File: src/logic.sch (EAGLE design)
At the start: 66 parts, among them CON1 CON-4P-TABS-JST_GH-RA, CON11 PINHEAD_1X04-2, CON12 PINHEAD_1X04-2, CON2 PINHEAD_1X04-2.54, CON3 PINHEAD_2X04-PLS-2, CON6 PINHEAD_2X02-PTH-2-MALE, CON7 PINHEAD_2X02-PTH-2-MALE, IC1 STM32F105RCT6, IC10 LM75-TSSOP8, IC11 LM75-TSSOP8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

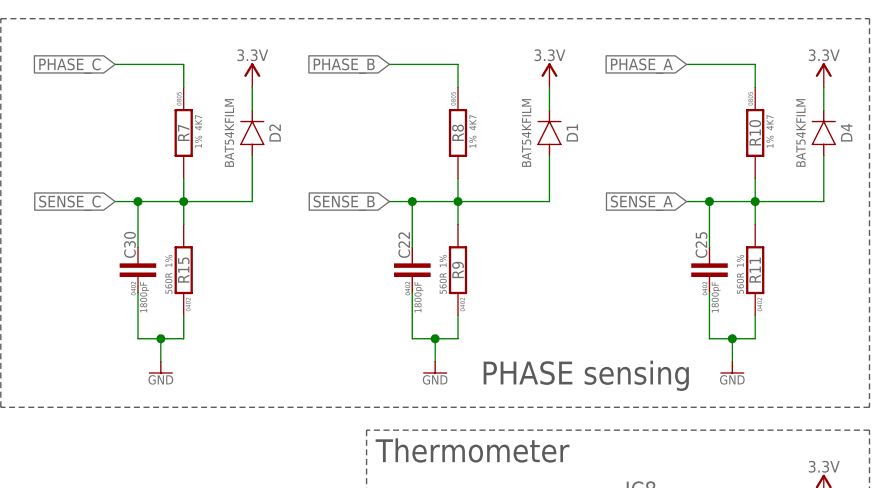
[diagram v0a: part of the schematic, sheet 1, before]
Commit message: BEMF sensig nets updates
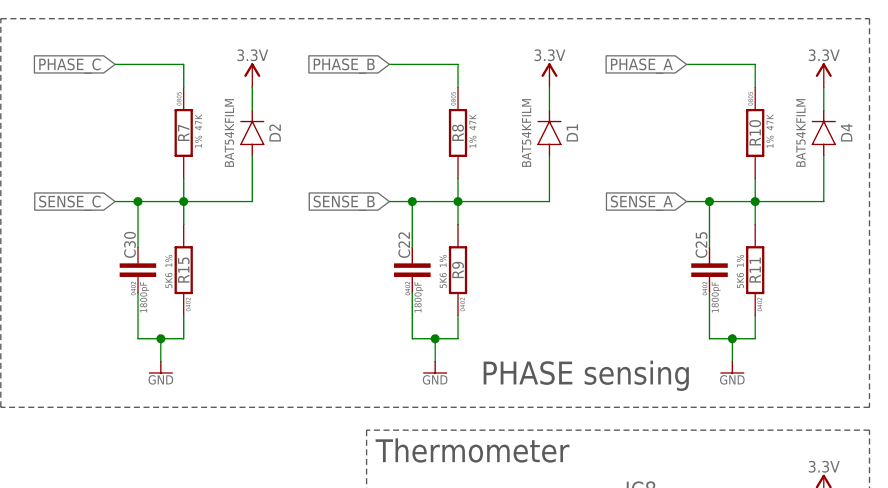
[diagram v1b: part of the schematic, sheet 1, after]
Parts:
- R10, R7, R8: value 4K7 -> 47K
- R11, R15, R9: value 560R -> 5K6
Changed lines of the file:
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@@
 </part>
 <part name="C30" library="rc" library_urn="urn:adsk.eagle:library:2539423" deviceset="C" device="-0402" package3d_urn="urn:adsk.eagle:package:2539461/2" value="1800pF"/>
-<part name="R7" library="rc" library_urn="urn:adsk.eagle:library:2539423" deviceset="R" device="-0805" package3d_urn="urn:adsk.eagle:package:2539455/2" technology="-1%" value="4K7"/>
-<part name="R15" library="rc" library_urn="urn:adsk.eagle:library:2539423" deviceset="R" device="-0402" package3d_urn="urn:adsk.eagle:package:2539456/2" technology="-1%" value="560R"/>
+<part name="R7" library="rc" library_urn="urn:adsk.eagle:library:2539423" deviceset="R" device="-0805" package3d_urn="urn:adsk.eagle:package:2539455/2" technology="-1%" value="47K"/>
+<part name="R15" library="rc" library_urn="urn:adsk.eagle:library:2539423" deviceset="R" device="-0402" package3d_urn="urn:adsk.eagle:package:2539456/2" technology="-1%" value="5K6"/>
 <part name="GND37" library="supply_symbols" library_urn="urn:adsk.eagle:library:13097679" deviceset="GND" device="" value="GND"/>
 <part name="C22" library="rc" library_urn="urn:adsk.eagle:library:2539423" deviceset="C" device="-0402" package3d_urn="urn:adsk.eagle:package:2539461/2" value="1800pF"/>
-<part name="R8" library="rc" library_urn="urn:adsk.eagle:library:2539423" deviceset="R" device="-0805" package3d_urn="urn:adsk.eagle:package:2539455/2" technology="-1%" value="4K7"/>
-<part name="R9" library="rc" library_urn="urn:adsk.eagle:library:2539423" deviceset="R" device="-0402" package3d_urn="urn:adsk.eagle:package:2539456/2" technology="-1%" value="560R"/>
+<part name="R8" library="rc" library_urn="urn:adsk.eagle:library:2539423" deviceset="R" device="-0805" package3d_urn="urn:adsk.eagle:package:2539455/2" technology="-1%" value="47K"/>
+<part name="R9" library="rc" library_urn="urn:adsk.eagle:library:2539423" deviceset="R" device="-0402" package3d_urn="urn:adsk.eagle:package:2539456/2" technology="-1%" value="5K6"/>
 <part name="GND26" library="supply_symbols" library_urn="urn:adsk.eagle:library:13097679" deviceset="GND" device="" value="GND"/>
 <part name="C25" library="rc" library_urn="urn:adsk.eagle:library:2539423" deviceset="C" device="-0402" package3d_urn="urn:adsk.eagle:package:2539461/2" value="1800pF"/>
-<part name="R10" library="rc" library_urn="urn:adsk.eagle:library:2539423" deviceset="R" device="-0805" package3d_urn="urn:adsk.eagle:package:2539455/2" technology="-1%" value="4K7"/>
-<part name="R11" library="rc" library_urn="urn:adsk.eagle:library:2539423" deviceset="R" device="-0402" package3d_urn="urn:adsk.eagle:package:2539456/2" technology="-1%" value="560R"/>
+<part name="R10" library="rc" library_urn="urn:adsk.eagle:library:2539423" deviceset="R" device="-0805" package3d_urn="urn:adsk.eagle:package:2539455/2" technology="-1%" value="47K"/>
+<part name="R11" library="rc" library_urn="urn:adsk.eagle:library:2539423" deviceset="R" device="-0402" package3d_urn="urn:adsk.eagle:package:2539456/2" technology="-1%" value="5K6"/>
 <part name="GND27" library="supply_symbols" library_urn="urn:adsk.eagle:library:13097679" deviceset="GND" device="" value="GND"/>
 <part name="+P7" library="supply_symbols" library_urn="urn:adsk.eagle:library:5017758" deviceset="3.3V" device=""/>

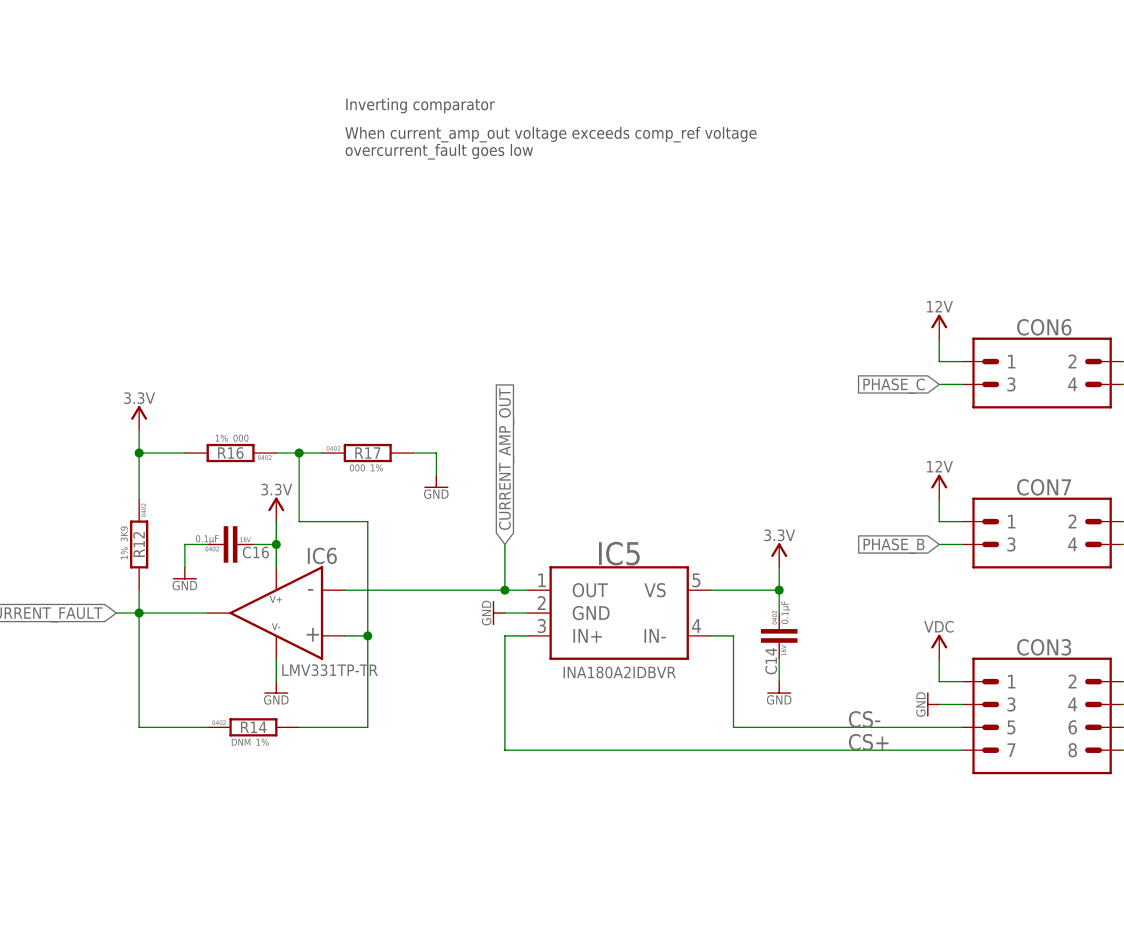
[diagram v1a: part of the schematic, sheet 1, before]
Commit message: Current amplifier input filtering added
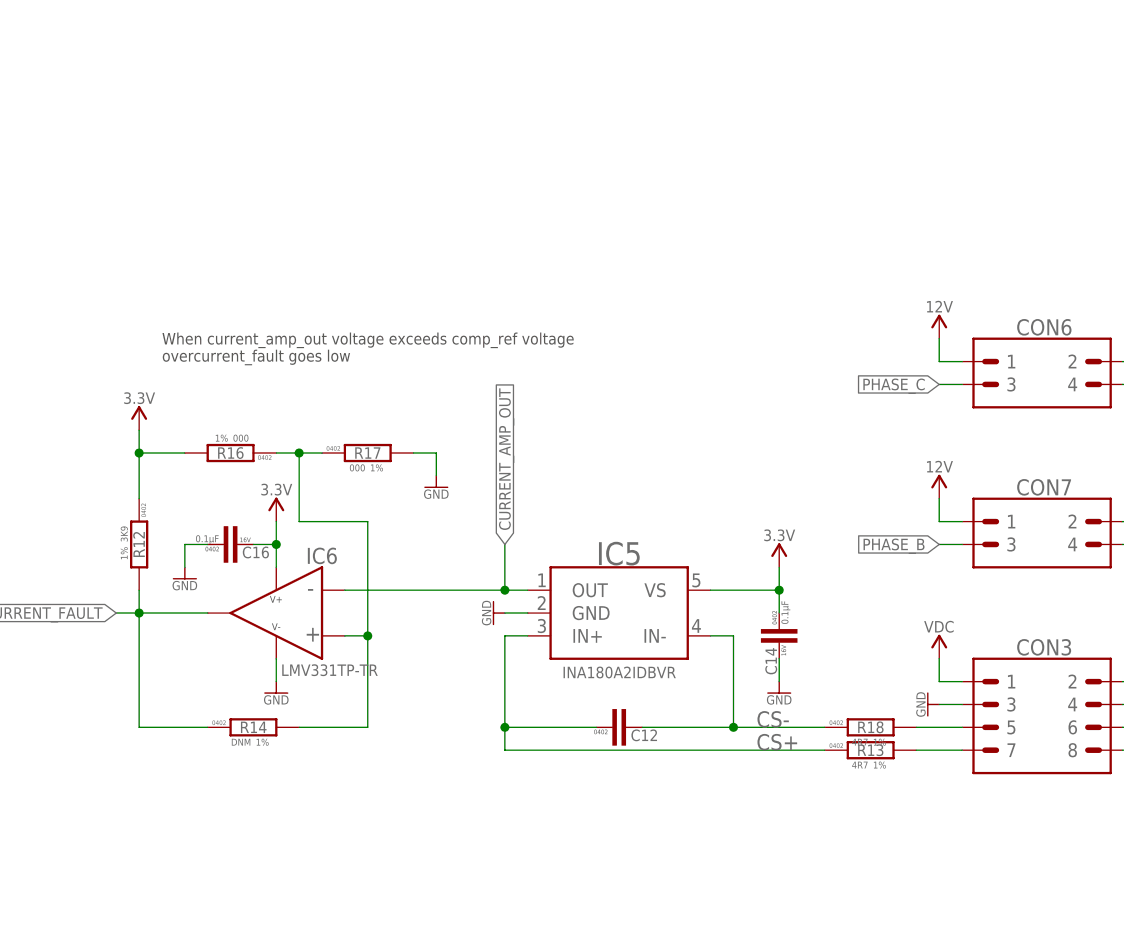
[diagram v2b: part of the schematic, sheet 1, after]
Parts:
- added C12: (no value), rc:C-0402
- added R13, R18: 4R7, rc:R-1%-0402
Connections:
- new net N$4: CON3.5, R18.2
- net CS+: now also C12.1, R13.1; no longer CON3.7
- net CS-: now also C12.2, R18.1; no longer CON3.5
- net N$1: now also CON3.7, R13.2
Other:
- note removed: "Inverting comparator"
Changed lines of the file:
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@@
 <part name="GND48" library="supply_symbols" library_urn="urn:adsk.eagle:library:13097679" deviceset="GND" device="" value="GND"/>
 <part name="+P15" library="supply_symbols" library_urn="urn:adsk.eagle:library:5017758" deviceset="5V" device=""/>
+<part name="R13" library="rc" library_urn="urn:adsk.eagle:library:2539423" deviceset="R" device="-0402" package3d_urn="urn:adsk.eagle:package:2539456/2" technology="-1%" value="4R7"/>
+<part name="R18" library="rc" library_urn="urn:adsk.eagle:library:2539423" deviceset="R" device="-0402" package3d_urn="urn:adsk.eagle:package:2539456/2" technology="-1%" value="4R7"/>
+<part name="C12" library="rc" library_urn="urn:adsk.eagle:library:2539423" deviceset="C" device="-0402" package3d_urn="urn:adsk.eagle:package:2539461/2"/>
 </parts>
 <sheets>
@@
 <text x="142.24" y="55.88" size="1.27" layer="97" font="vector">Place R26 TO WRITE PROTECT</text>
 <text x="142.24" y="33.02" size="1.778" layer="97">WP pin pull up is optional</text>
-<text x="129.54" y="243.84" size="1.27" layer="97" font="vector">Inverting comparator</text>
-<text x="129.54" y="238.76" size="1.27" layer="97" font="vector">When current_amp_out voltage exceeds comp_ref voltage
+<text x="109.22" y="215.9" size="1.27" layer="97" font="vector">When current_amp_out voltage exceeds comp_ref voltage
 overcurrent_fault goes low</text>
 </plain>
@@
 <instance part="GND44" gate="1" x="139.7" y="203.2" smashed="yes">
 <attribute name="VALUE" x="139.7" y="201.168" size="1.016" layer="96" font="vector" ratio="15" align="center"/>
+</instance>
+<instance part="R13" gate="G$1" x="187.96" y="172.72" smashed="yes">
+<attribute name="NAME" x="187.96" y="172.72" size="1.27" layer="95" font="vector" align="center"/>
+<attribute name="VALUE" x="187.706" y="170.688" size="0.762" layer="96" font="vector" align="bottom-right"/>
+<attribute name="PACKAGE" x="184.15" y="173.228" size="0.508" layer="95" font="vector" align="center"/>
+<attribute name="TOLERANCE" x="188.214" y="170.688" size="0.762" layer="96" font="vector"/>
+</instance>
+<instance part="R18" gate="G$1" x="187.96" y="175.26" smashed="yes">
+<attribute name="NAME" x="187.96" y="175.26" size="1.27" layer="95" font="vector" align="center"/>
+<attribute name="VALUE" x="187.706" y="173.228" size="0.762" layer="96" font="vector" align="bottom-right"/>
+<attribute name="PACKAGE" x="184.15" y="175.768" size="0.508" layer="95" font="vector" align="center"/>
+<attribute name="TOLERANCE" x="188.214" y="173.228" size="0.762" layer="96" font="vector"/>
+</instance>
+<instance part="C12" gate="G$1" x="160.02" y="175.26" smashed="yes">
+<attribute name="NAME" x="161.29" y="174.371" size="1.27" layer="95" font="vector" align="center-left"/>
+<attribute name="VALUE" x="158.75" y="175.514" size="0.762" layer="96" font="vector" align="bottom-right"/>
+<attribute name="PACKAGE" x="157.988" y="174.752" size="0.508" layer="97" font="vector" rot="R180" align="center"/>
+<attribute name="VOLTAGE" x="161.036" y="175.768" size="0.508" layer="97" font="vector" align="center-left"/>
 </instance>
 </instances>
@@
 <net name="CS+" class="0">
 <segment>
-<pinref part="CON3" gate="G$1" pin="7"/>
 <pinref part="IC5" gate="G$1" pin="IN+"/>
 <wire x1="149.86" y1="185.42" x2="147.32" y2="185.42" width="0.1524" layer="91"/>
-<wire x1="198.12" y1="172.72" x2="147.32" y2="172.72" width="0.1524" layer="91"/>
-<wire x1="147.32" y1="172.72" x2="147.32" y2="185.42" width="0.1524" layer="91"/>
-<label x="185.42" y="172.72" size="1.778" layer="95"/>
+<wire x1="147.32" y1="172.72" x2="147.32" y2="175.26" width="0.1524" layer="91"/>
+<label x="175.26" y="172.72" size="1.778" layer="95"/>
+<wire x1="147.32" y1="175.26" x2="147.32" y2="185.42" width="0.1524" layer="91"/>
+<wire x1="182.88" y1="172.72" x2="147.32" y2="172.72" width="0.1524" layer="91"/>
+<pinref part="R13" gate="G$1" pin="1"/>
+<pinref part="C12" gate="G$1" pin="1"/>
+<wire x1="157.48" y1="175.26" x2="147.32" y2="175.26" width="0.1524" layer="91"/>
+<junction x="147.32" y="175.26"/>
 </segment>
 </net>
 <net name="CS-" class="0">
 <segment>
-<pinref part="CON3" gate="G$1" pin="5"/>
 <pinref part="IC5" gate="G$1" pin="IN-"/>
 <wire x1="170.18" y1="185.42" x2="172.72" y2="185.42" width="0.1524" layer="91"/>
 <wire x1="172.72" y1="185.42" x2="172.72" y2="175.26" width="0.1524" layer="91"/>
-<wire x1="198.12" y1="175.26" x2="172.72" y2="175.26" width="0.1524" layer="91"/>
-<label x="185.42" y="175.26" size="1.778" layer="95"/>
+<label x="175.26" y="175.26" size="1.778" layer="95"/>
+<wire x1="182.88" y1="175.26" x2="172.72" y2="175.26" width="0.1524" layer="91"/>
+<pinref part="R18" gate="G$1" pin="1"/>
+<pinref part="C12" gate="G$1" pin="2"/>
+<wire x1="162.56" y1="175.26" x2="172.72" y2="175.26" width="0.1524" layer="91"/>
+<junction x="172.72" y="175.26"/>
 </segment>
 </net>
@@
 </segment>
 </net>
+<net name="N$1" class="0">
+<segment>
+<pinref part="CON3" gate="G$1" pin="7"/>
+<wire x1="198.12" y1="172.72" x2="193.04" y2="172.72" width="0.1524" layer="91"/>
+<pinref part="R13" gate="G$1" pin="2"/>
+</segment>
+</net>
+<net name="N$4" class="0">
+<segment>
+<pinref part="CON3" gate="G$1" pin="5"/>
+<wire x1="198.12" y1="175.26" x2="193.04" y2="175.26" width="0.1524" layer="91"/>
+<pinref part="R18" gate="G$1" pin="2"/>
+</segment>
+</net>

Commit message: Logic PCB  updates
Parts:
- removed R14: DNM, rc:R-1%-0402
- added D3: BAT54KFILM, Diodes:BAT54KFILM
- added RFB: DNM, rc:R-1%-0603
- C15: value 0.1µF -> 2200pF
- R12: value 3K9 -> 5K6
- R16: value 000 -> 3K3
- R17: value 000 -> 5K6
- R5: value (none) -> 60K
- R6: value (none) -> 2K
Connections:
- new net VREF: IC6.IN+, R16.1, R17.1, RFB.2
- net N$2: no longer IC6.IN+, R14.2, R16.1, R17.1
- net OVERCURRENT_FAULT: now also RFB.1; no longer R14.1
- net SENSE_VIN: now also D3.A
- net VDD_3V3: now also D3.C
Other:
- note added: "Overcurrent event is detected once CURRENT_AMP_OUT voltage exceeds Vref = G*I*Rshunt Vref = 50*200*0.0002 = 2 V"
- note added: "Real Vref = 5.6/(5.6+3.3) * 3.3 = 2.07 V"
- moved on the sheet: C15, R17, R5, R6

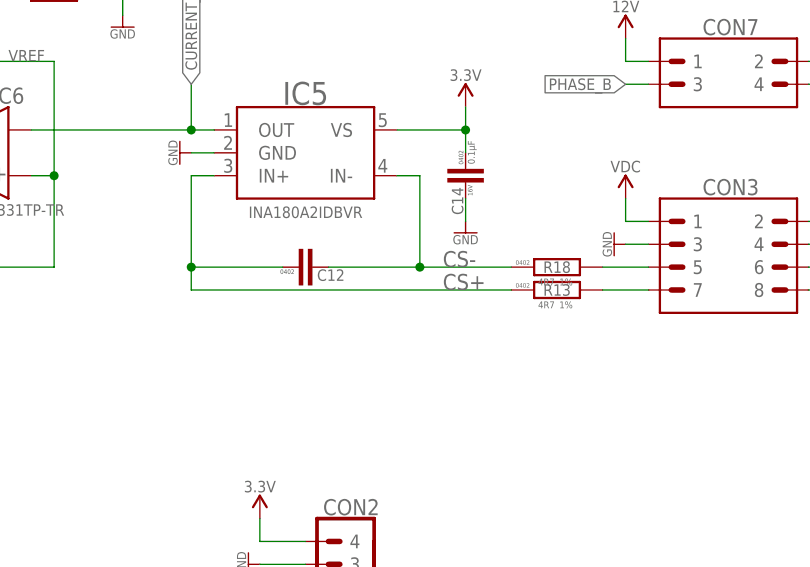
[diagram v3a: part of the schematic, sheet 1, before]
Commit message: Values of the current amp filter  updated
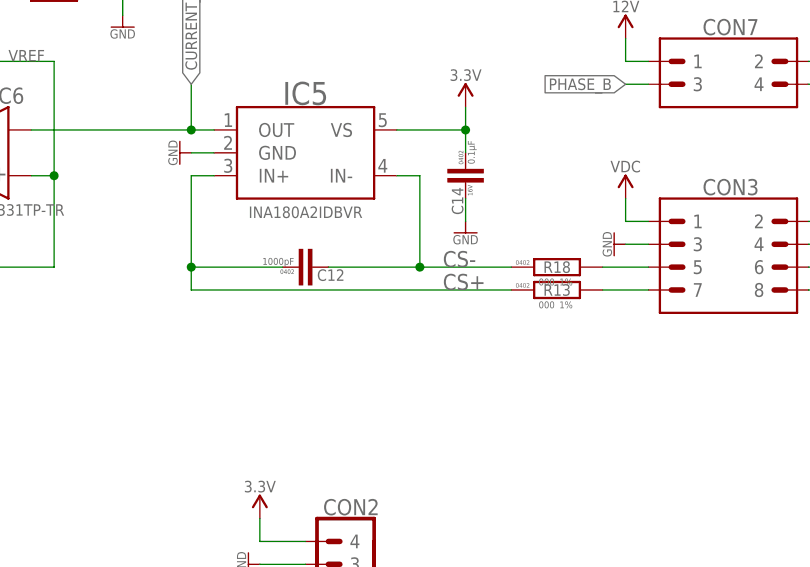
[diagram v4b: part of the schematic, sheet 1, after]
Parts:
- C12: value (none) -> 1000pF
- R13, R18: value 4R7 -> 000
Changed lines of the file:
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@@
 <part name="GND48" library="supply_symbols" library_urn="urn:adsk.eagle:library:13097679" deviceset="GND" device="" value="GND"/>
 <part name="+P15" library="supply_symbols" library_urn="urn:adsk.eagle:library:5017758" deviceset="5V" device=""/>
-<part name="R13" library="rc" library_urn="urn:adsk.eagle:library:2539423" deviceset="R" device="-0402" package3d_urn="urn:adsk.eagle:package:2539456/2" technology="-1%" value="4R7"/>
-<part name="R18" library="rc" library_urn="urn:adsk.eagle:library:2539423" deviceset="R" device="-0402" package3d_urn="urn:adsk.eagle:package:2539456/2" technology="-1%" value="4R7"/>
-<part name="C12" library="rc" library_urn="urn:adsk.eagle:library:2539423" deviceset="C" device="-0402" package3d_urn="urn:adsk.eagle:package:2539461/2"/>
+<part name="R13" library="rc" library_urn="urn:adsk.eagle:library:2539423" deviceset="R" device="-0402" package3d_urn="urn:adsk.eagle:package:2539456/2" technology="-1%" value="000"/>
+<part name="R18" library="rc" library_urn="urn:adsk.eagle:library:2539423" deviceset="R" device="-0402" package3d_urn="urn:adsk.eagle:package:2539456/2" technology="-1%" value="000"/>
+<part name="C12" library="rc" library_urn="urn:adsk.eagle:library:2539423" deviceset="C" device="-0402" package3d_urn="urn:adsk.eagle:package:2539461/2" value="1000pF"/>
 <part name="D3" library="Diodes" library_urn="urn:adsk.eagle:library:2473263" deviceset="BAT54KFILM" device="" package3d_urn="urn:adsk.eagle:package:1040205/3"/>
 <part name="+P14" library="supply_symbols" library_urn="urn:adsk.eagle:library:5017758" deviceset="3.3V" device=""/>
